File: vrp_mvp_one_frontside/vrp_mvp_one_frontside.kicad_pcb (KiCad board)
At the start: 2 copper layers, 77 x 150 mm, 88 parts, among them J1 Micro_SD_Card, J2 BACKSIDE_INTERFACE_1, J4 USB_C_Receptacle_USB2.0_16P, J6 DEBUG, J7 BACKSIDE_INTERFACE_2, J8 SJ3-35094BG, Q1 MMBT2222A, Q2 MMBT2222A, Q3 MMBT2222A, SW1 SEND, SW10 TWO, SW11 THREE, SW12 FOUR, SW13 FIVE, SW14 SIX, SW15 SEVEN, SW16 EIGHT, SW17 NINE, SW18 ALPHA, SW19 BETA, SW2 END, SW20 ZERO, SW21 RESET, SW3 PAGE, SW4 CLR, SW5 POUND, SW6 UP, SW7 DOWN, SW8 ASTERISK, SW9 ONE, U2 NHD-C0220BIZ, U3 ATSAMD21G18A-A, U4 TLV320AIC3104IRHBT, U5 SN74CB3Q3257PWR

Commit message: response to issue 1
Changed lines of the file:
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@@
 		(property "Value" "SEND"
 			(at 3.75 6.7 0)
-			(layer "F.SilkS")
+			(layer "F.SilkS" knockout)
 			(effects
 				(font
@@
 		(property "Value" "PAGE"
 			(at 3.75 6.7 0)
-			(layer "F.SilkS")
+			(layer "F.SilkS" knockout)
 			(effects
 				(font
@@
 		)
 		(property "Value" "SIX"
-			(at 3.75 6.2 0)
-			(layer "F.SilkS")
+			(at 3.75 6.75 0)
+			(layer "F.SilkS" knockout)
 			(effects
 				(font
@@
 		(property "Value" "EIGHT"
 			(at 3.75 6.95 0)
-			(layer "F.SilkS")
+			(layer "F.SilkS" knockout)
 			(effects
 				(font
@@
 		(property "Value" "TWO"
 			(at 3.75 6.7 0)
-			(layer "F.SilkS")
+			(layer "F.SilkS" knockout)
 			(effects
 				(font
@@
 		(property "Value" "END"
 			(at 3.75 6.7 0)
-			(layer "F.SilkS")
+			(layer "F.SilkS" knockout)
 			(effects
 				(font
@@
 		(property "Value" "ALPHA"
 			(at 3.75 6.7 0)
-			(layer "F.SilkS")
+			(layer "F.SilkS" knockout)
 			(effects
 				(font
@@
 		(at 121.7 29)
 		(property "Reference" "LS1"
-			(at 3.175 -8.885 0)
+			(at 0 0 0)
 			(layer "F.SilkS")
 			(effects
@@
 		(property "Value" "ZERO"
 			(at 3.75 6.7 0)
-			(layer "F.SilkS")
+			(layer "F.SilkS" knockout)
 			(effects
 				(font
@@
 		(property "Value" "UP"
 			(at 3.75 6.7 0)
-			(layer "F.SilkS")
+			(layer "F.SilkS" knockout)
 			(effects
 				(font
@@
 		(property "Value" "CLR"
 			(at 3.75 6.7 0)
-			(layer "F.SilkS")
+			(layer "F.SilkS" knockout)
 			(effects
 				(font
@@
 		)
 		(property "Value" "RESET"
-			(at 3.75 6.7 0)
-			(layer "F.SilkS")
+			(at 3 6.7 0)
+			(layer "F.SilkS" knockout)
 			(effects
 				(font
 					(size 1 1)
-					(thickness 0.15)
+					(thickness 0.2)
+					(bold yes)
 				)
 			)
@@
 		)
 		(property "Value" "BETA"
-			(at 3.75 6.2 0)
-			(layer "F.SilkS")
+			(at 3.75 6.75 0)
+			(layer "F.SilkS" knockout)
 			(effects
 				(font
@@
 		(property "Value" "NINE"
 			(at 3.75 6.95 0)
-			(layer "F.SilkS")
+			(layer "F.SilkS" knockout)
 			(effects
 				(font
@@
 		(property "Value" "SEVEN"
 			(at 3.75 6.95 0)
-			(layer "F.SilkS")
+			(layer "F.SilkS" knockout)
 			(effects
 				(font
@@
 		(property "Value" "POUND"
 			(at 3.75 6.7 0)
-			(layer "F.SilkS")
+			(layer "F.SilkS" knockout)
 			(effects
 				(font
@@
 		)
 		(property "Value" "FOUR"
-			(at 3.75 6.2 0)
-			(layer "F.SilkS")
+			(at 3.75 6.75 0)
+			(layer "F.SilkS" knockout)
 			(effects
 				(font
@@
 		)
 		(property "Value" "FIVE"
-			(at 3.75 6.2 0)
-			(layer "F.SilkS")
+			(at 3.75 6.75 0)
+			(layer "F.SilkS" knockout)
 			(effects
 				(font
@@
 		(property "Value" "ASTERISK"
 			(at 3.75 6.7 0)
-			(layer "F.SilkS")
+			(layer "F.SilkS" knockout)
 			(effects
 				(font
@@
 		(property "Value" "DOWN"
 			(at 3.75 6.7 0)
-			(layer "F.SilkS")
+			(layer "F.SilkS" knockout)
 			(effects
 				(font
@@
 		(property "Value" "THREE"
 			(at 3.75 6.7 0)
-			(layer "F.SilkS")
+			(layer "F.SilkS" knockout)
 			(effects
 				(font
@@
 		(property "Value" "ONE"
 			(at 3.75 6.7 0)
-			(layer "F.SilkS")
+			(layer "F.SilkS" knockout)
 			(effects
 				(font
@@
 	(gr_text "GND"
 		(at 103.5 106.5 90)
-		(layer "F.SilkS")
+		(layer "F.SilkS" knockout)
 		(effects
 			(font
 				(size 1 1)
-				(thickness 0.125)
+				(thickness 0.2)
+				(bold yes)
 			)
 			(justify left bottom)
@@
 	(gr_text "STATUS"
 		(at 102 22.5 0)
-		(layer "F.SilkS")
+		(layer "F.SilkS" knockout)
 		(effects
 			(font
 				(size 1 1)
-				(thickness 0.125)
+				(thickness 0.2)
+				(bold yes)
 			)
 			(justify left bottom)
@@
 	(gr_text "SDIO"
 		(at 96 106.5 90)
-		(layer "F.SilkS")
+		(layer "F.SilkS" knockout)
 		(effects
 			(font
 				(size 1 1)
-				(thickness 0.125)
+				(thickness 0.2)
+				(bold yes)
 			)
 			(justify left bottom)
@@
 	(gr_text "3.3V"
 		(at 101 106.5 90)
-		(layer "F.SilkS")
+		(layer "F.SilkS" knockout)
 		(effects
 			(font
 				(size 1 1)
-				(thickness 0.125)
+				(thickness 0.2)
+				(bold yes)
 			)
 			(justify left bottom)
@@
 	(gr_text "SWCLK"
 		(at 98.5 106.5 90)
-		(layer "F.SilkS")
+		(layer "F.SilkS" knockout)
 		(effects
 			(font
 				(size 1 1)
-				(thickness 0.125)
+				(thickness 0.2)
+				(bold yes)
 			)
 			(justify left bottom)

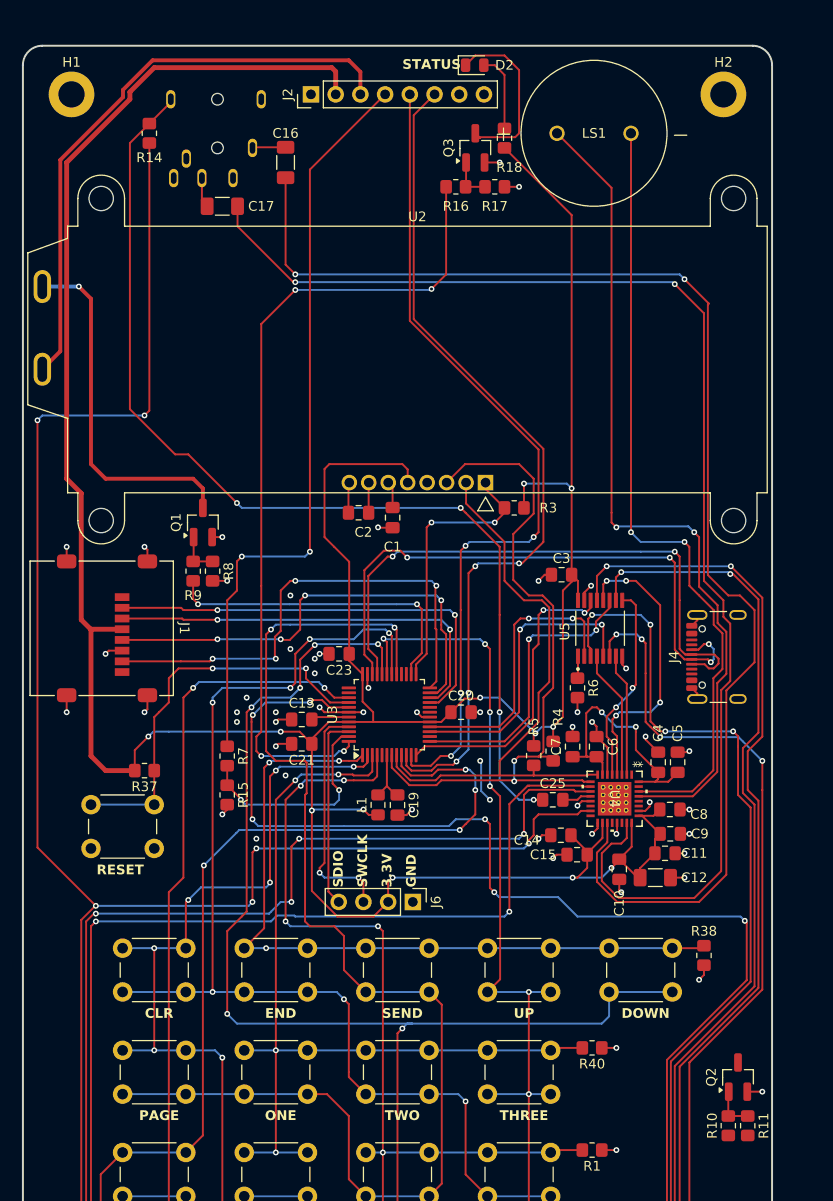
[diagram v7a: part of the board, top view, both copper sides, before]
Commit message: removed vibration motor circuitry
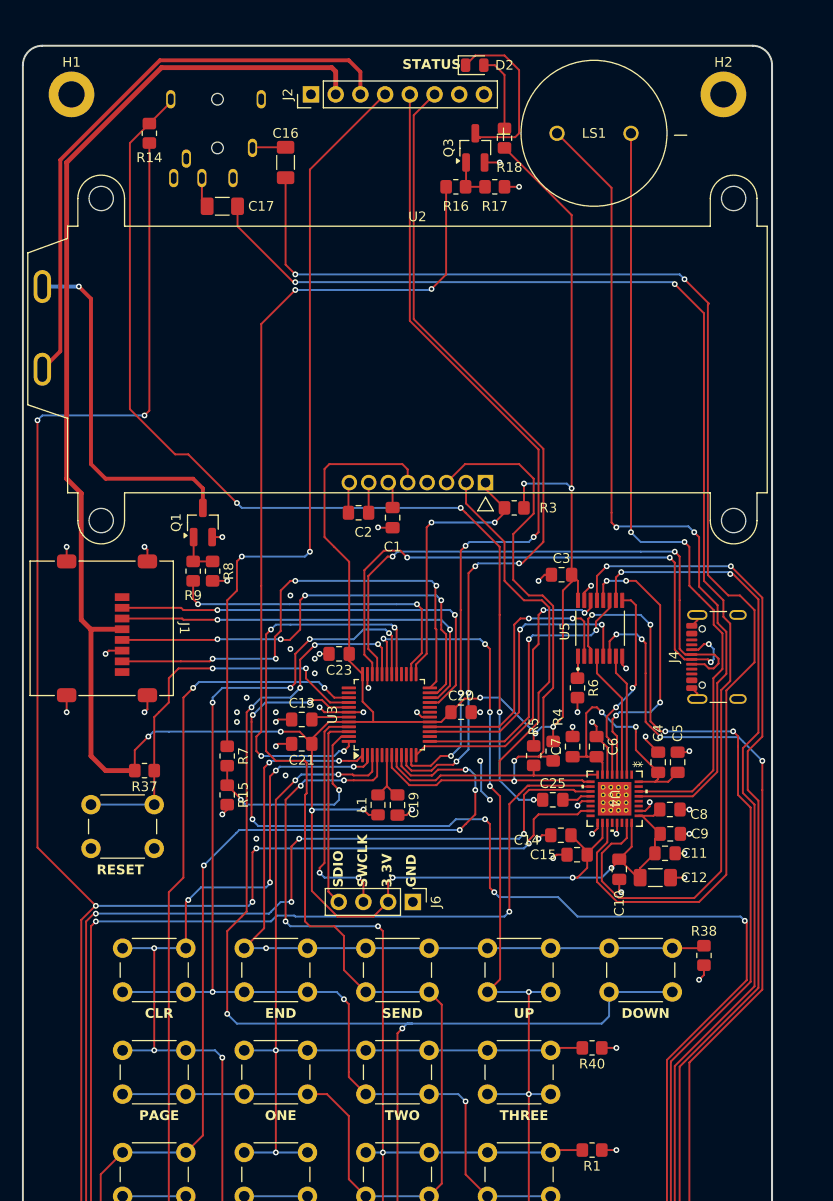
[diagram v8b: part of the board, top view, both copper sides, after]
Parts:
- removed Q2: MMBT2222A, Package_TO_SOT_SMD:SOT-23_Handsoldering
- removed R10: 100, Resistor_SMD:R_0805_2012Metric_Pad1.20x1.40mm_HandSolder
- removed R11: 10K, Resistor_SMD:R_0805_2012Metric_Pad1.20x1.40mm_HandSolder
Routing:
- net Net-(Q2-B): track 4.52 -> 0.00 mm
- net GND: track 81.1 -> 79.5 mm, vias 58 -> 57
